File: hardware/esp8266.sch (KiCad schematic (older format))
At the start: 34 parts

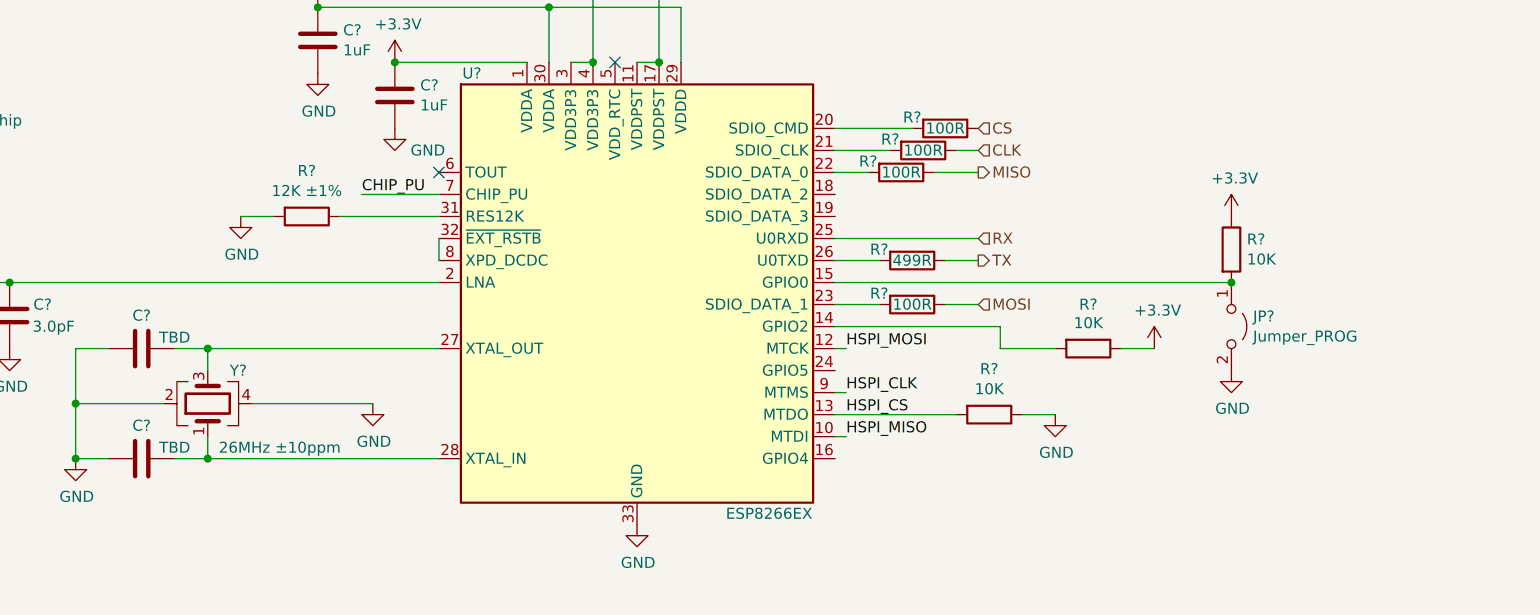
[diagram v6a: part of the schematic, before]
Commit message: Select crystals, add HSE for stm32 and fixed some bits
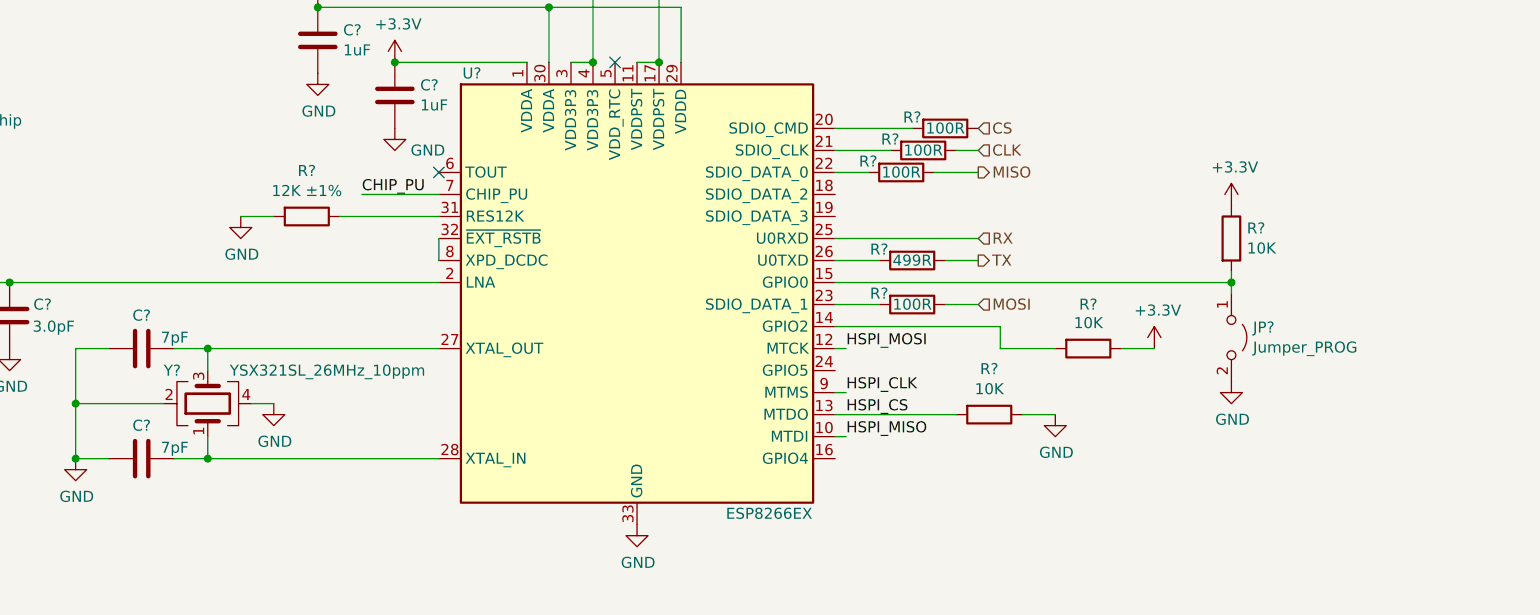
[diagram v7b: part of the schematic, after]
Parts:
- C? (x2): value TBD -> 7pF
- Y?: value 26MHz ±10ppm -> YSX321SL_26MHz_10ppm; footprint (none) -> Crystal:Crystal_SMD_3225-4Pin_3.2x2.5mm
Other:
- moved on the sheet: JP?, R?
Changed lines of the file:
@@
 encoding utf-8
 Sheet 2 5
-Title ""
+Title "Meteostation"
 Date ""
 Rev ""
-Comp ""
+Comp "Technospark"
 Comment1 ""
-Comment2 ""
+Comment2 "Aleksul"
 Comment3 ""
 Comment4 ""
@@
 U 1 1 6032C197
 P 2800 3800
-F 0 "Y?" V 2950 3700 50  0000 R CNN
-F 1 "26MHz ±10ppm" V 2600 3750 50  0000 R CNN
-F 2 "" H 2800 3800 50  0001 C CNN
+F 0 "Y?" V 2950 4000 50  0000 R CNN
+F 1 "YSX321SL_26MHz_10ppm" V 2950 3700 50  0000 R CNN
+F 2 "Crystal:Crystal_SMD_3225-4Pin_3.2x2.5mm" H 2800 3800 50  0001 C CNN
 F 3 "~" H 2800 3800 50  0001 C CNN
 	1    2800 3800
@@
 L power:GND #PWR0113
 U 1 1 60333C6B
-P 3550 3800
-F 0 "#PWR0113" H 3550 3550 50  0001 C CNN
-F 1 "GND" H 3555 3627 50  0000 C CNN
-F 2 "" H 3550 3800 50  0001 C CNN
-F 3 "" H 3550 3800 50  0001 C CNN
-	1    3550 3800
+P 3100 3800
+F 0 "#PWR0113" H 3100 3550 50  0001 C CNN
+F 1 "GND" H 3105 3627 50  0000 C CNN
+F 2 "" H 3100 3800 50  0001 C CNN
+F 3 "" H 3100 3800 50  0001 C CNN
+	1    3100 3800
 	1    0    0    -1
 $EndComp
@@
 $EndComp
 Wire Wire Line
-	3000 3800 3550 3800
+	3000 3800 3100 3800
 Wire Wire Line
 	4750 2250 4850 2250
@@
 P 2500 4050
 F 0 "C?" V 2350 4050 50  0000 C CNN
-F 1 "TBD" V 2450 4200 50  0000 C CNN
+F 1 "7pF" V 2450 4200 50  0000 C CNN
 F 2 "" H 2538 3900 50  0001 C CNN
 F 3 "~" H 2500 4050 50  0001 C CNN
@@
 P 2500 3550
 F 0 "C?" V 2350 3550 50  0000 C CNN
-F 1 "TBD" V 2450 3700 50  0000 C CNN
+F 1 "7pF" V 2450 3700 50  0000 C CNN
 F 2 "" H 2538 3400 50  0001 C CNN
 F 3 "~" H 2500 3550 50  0001 C CNN
@@
 L Device:R R?
 U 1 1 6037BDBF
-P 7450 3100
-F 0 "R?" H 7520 3146 50  0000 L CNN
-F 1 "10K" H 7520 3055 50  0000 L CNN
-F 2 "" V 7380 3100 50  0001 C CNN
-F 3 "~" H 7450 3100 50  0001 C CNN
-	1    7450 3100
+P 7450 3050
+F 0 "R?" H 7520 3096 50  0000 L CNN
+F 1 "10K" H 7520 3005 50  0000 L CNN
+F 2 "" V 7380 3050 50  0001 C CNN
+F 3 "~" H 7450 3050 50  0001 C CNN
+	1    7450 3050
 	1    0    0    -1
 $EndComp
@@
 L Jumper:Jumper_2_Open JP?
 U 1 1 603825B2
-P 7450 3450
-F 0 "JP?" V 7404 3548 50  0000 L CNN
-F 1 "Jumper_PROG" V 7495 3548 50  0000 L CNN
-F 2 "" H 7450 3450 50  0001 C CNN
-F 3 "~" H 7450 3450 50  0001 C CNN
-	1    7450 3450
+P 7450 3500
+F 0 "JP?" V 7404 3598 50  0000 L CNN
+F 1 "Jumper_PROG" V 7495 3598 50  0000 L CNN
+F 2 "" H 7450 3500 50  0001 C CNN
+F 3 "~" H 7450 3500 50  0001 C CNN
+	1    7450 3500
 	0    1    1    0
 $EndComp
@@
 L power:+3.3V #PWR0130
 U 1 1 60390ADA
-P 7450 2950
-F 0 "#PWR0130" H 7450 2800 50  0001 C CNN
-F 1 "+3.3V" H 7465 3123 50  0000 C CNN
-F 2 "" H 7450 2950 50  0001 C CNN
-F 3 "" H 7450 2950 50  0001 C CNN
-	1    7450 2950
+P 7450 2900
+F 0 "#PWR0130" H 7450 2750 50  0001 C CNN
+F 1 "+3.3V" H 7465 3073 50  0000 C CNN
+F 2 "" H 7450 2900 50  0001 C CNN
+F 3 "" H 7450 2900 50  0001 C CNN
+	1    7450 2900
 	1    0    0    -1
 $EndComp
@@
 L power:GND #PWR0131
 U 1 1 60391528
-P 7450 3650
-F 0 "#PWR0131" H 7450 3400 50  0001 C CNN
-F 1 "GND" H 7455 3477 50  0000 C CNN
-F 2 "" H 7450 3650 50  0001 C CNN
-F 3 "" H 7450 3650 50  0001 C CNN
-	1    7450 3650
+P 7450 3700
+F 0 "#PWR0131" H 7450 3450 50  0001 C CNN
+F 1 "GND" H 7455 3527 50  0000 C CNN
+F 2 "" H 7450 3700 50  0001 C CNN
+F 3 "" H 7450 3700 50  0001 C CNN
+	1    7450 3700
 	1    0    0    -1
 $EndComp
@@
 Wire Wire Line
 	10000 5650 10050 5650
-Connection ~ 7450 3250
 Wire Wire Line
 	5650 3450 6400 3450
@@
 Wire Wire Line
 	1900 3250 3850 3250
+Wire Wire Line
+	7450 3300 7450 3250
+Wire Wire Line
+	7450 3200 7450 3250
+Connection ~ 7450 3250
 $EndSCHEMATC

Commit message: Annotation complete
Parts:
- gave numbers to parts that had none: 34
